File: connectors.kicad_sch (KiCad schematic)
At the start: 44 parts, among them J6 10107844-002LF, J7 JST_XH_1x2_S2B-XH-A-LF-SN, Q5 BC807-25W, SW1 MSS3-V-T_R, U8 USB4145-03-0070-c_REVA2

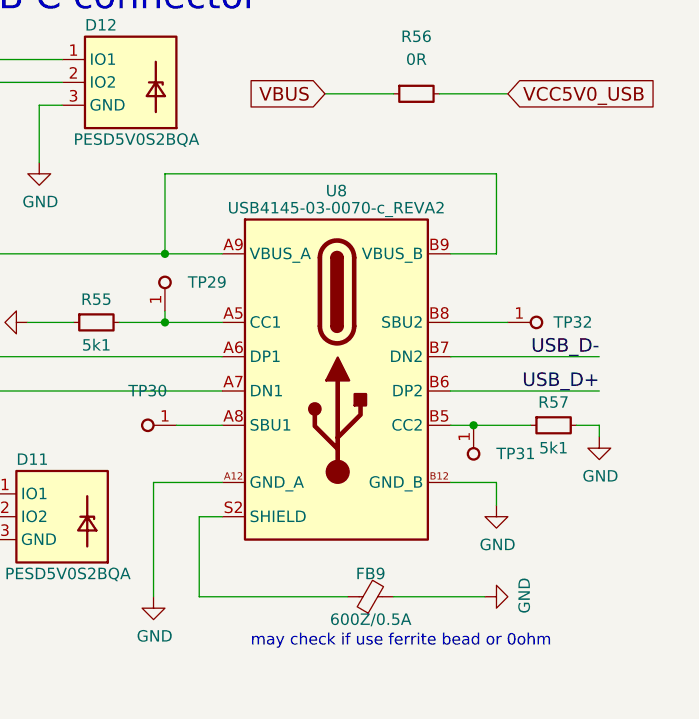
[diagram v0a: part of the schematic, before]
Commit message: Standarize all components and enumerate
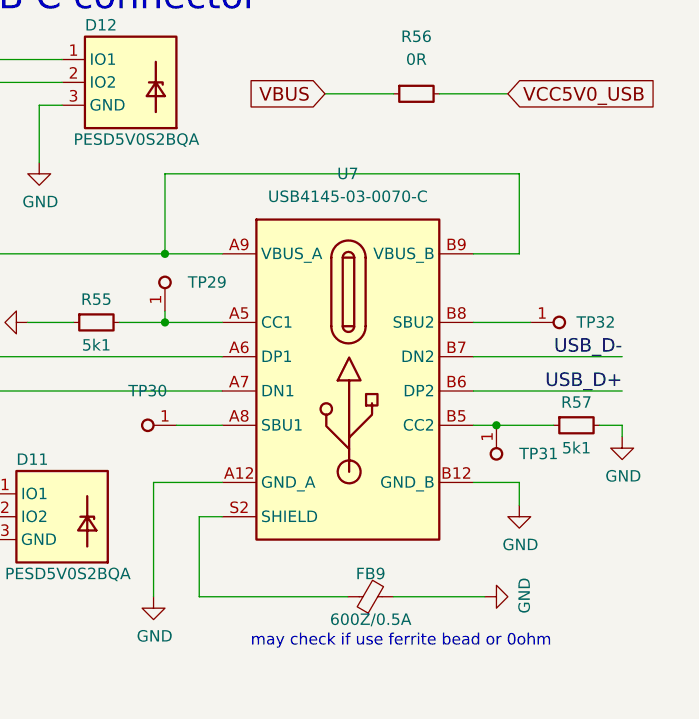
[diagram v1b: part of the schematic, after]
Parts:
- removed U8: USB4145-03-0070-c_REVA2, antmicro-footprints:GCT_USB4145-03-0070-C_REVA, symbol antmicroUSBDVIHDMIConnectors:USB4145-03-0070-c_REVA
- added U7: USB-C_GCT_USB4145-03-0070-C, antmicro-footprints:GCT_USB4145-03-0070-C_REVA, symbol antmicroUSBConnectors:USB-C_GCT_USB4145-03-0070-C
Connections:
- net GND: now also U7.A12 (GND_A), U7.B12 (GND_B)
- net USB_D+: now also U7.A6 (DP1), U7.B6 (DP2)
- net USB_D-: now also U7.A7 (DN1), U7.B7 (DN2)
- net VBUS: now also U7.A9 (VBUS_A), U7.B9 (VBUS_B)
- net at TP32.1: now also U7.B8 (SBU2)
- net at TP30.1: now also U7.A8 (SBU1)
- net at R57.1, TP31.1: now also U7.B5 (CC2)
- net at R55.2, TP29.1: now also U7.A5 (CC1)
- net at FB9.1: now also U7.S2 (SHIELD)
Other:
- moved on the sheet: R57, TP31, TP32

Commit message: Reannotate
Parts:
- renumbered C35 to C38, Q5 to Q8, R50 to R58, R51 to R59, R52 to R60, R53 to R61, R54 to R62, R55 to R63, R56 to R64, R57 to R65, U7 to U10
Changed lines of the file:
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@@
   (symbol (lib_id "antmicroResistorsmisc:R_0R_0805") (at 91.44 179.07 0) (unit 1)
     (in_bom yes) (on_board yes)
-    (property "Reference" "R50" (id 0) (at 93.98 173.99 0)
+    (property "Reference" "R58" (id 0) (at 93.98 173.99 0)
       (effects (font (size 1.27 1.27) (thickness 0.15)))
     )
@@
   (symbol (lib_id "antmicropower:GND") (at 373.38 144.78 0) (unit 1)
     (in_bom yes) (on_board yes)
-    (property "Reference" "#PWR0107" (id 0) (at 373.38 151.13 0)
+    (property "Reference" "#PWR0125" (id 0) (at 373.38 151.13 0)
       (effects (font (size 1.27 1.27)) hide)
     )
@@
   (symbol (lib_id "antmicropower:+3V3") (at 218.44 113.03 0) (unit 1)
     (in_bom yes) (on_board yes) (fields_autoplaced)
-    (property "Reference" "#PWR098" (id 0) (at 233.68 115.57 0)
+    (property "Reference" "#PWR0116" (id 0) (at 233.68 115.57 0)
       (effects (font (size 1.27 1.27) (thickness 0.15)) (justify left bottom) hide)
     )
@@
   (symbol (lib_id "antmicroUSBConnectors:USB-C_GCT_USB4145-03-0070-C") (at 328.93 124.46 0) (unit 1)
     (in_bom yes) (on_board yes) (fields_autoplaced)
-    (property "Reference" "U7" (id 0) (at 342.9 115.57 0)
+    (property "Reference" "U10" (id 0) (at 342.9 115.57 0)
       (effects (font (size 1.27 1.27) (thickness 0.15)))
     )
@@
   (symbol (lib_name "R_0R_0402_2") (lib_id "antmicroResistors0402:R_0R_0402") (at 194.31 143.51 0) (unit 1)
     (in_bom yes) (on_board yes)
-    (property "Reference" "R52" (id 0) (at 196.85 139.7 0)
+    (property "Reference" "R60" (id 0) (at 196.85 139.7 0)
       (effects (font (size 1.27 1.27) (thickness 0.15)))
     )
@@
   (symbol (lib_id "antmicropower:GND") (at 123.19 118.11 0) (unit 1)
     (in_bom yes) (on_board yes)
-    (property "Reference" "#PWR095" (id 0) (at 123.19 124.46 0)
+    (property "Reference" "#PWR0113" (id 0) (at 123.19 124.46 0)
       (effects (font (size 1.27 1.27)) hide)
     )
@@
   (symbol (lib_id "antmicropower:GND") (at 300.99 162.56 0) (unit 1)
     (in_bom yes) (on_board yes)
-    (property "Reference" "#PWR0101" (id 0) (at 300.99 168.91 0)
+    (property "Reference" "#PWR0119" (id 0) (at 300.99 168.91 0)
       (effects (font (size 1.27 1.27)) hide)
     )
@@
   (symbol (lib_id "antmicropower:GND") (at 307.34 132.08 270) (unit 1)
     (in_bom yes) (on_board yes)
-    (property "Reference" "#PWR0102" (id 0) (at 300.99 132.08 0)
+    (property "Reference" "#PWR0120" (id 0) (at 300.99 132.08 0)
       (effects (font (size 1.27 1.27)) hide)
     )
@@
   (symbol (lib_name "R_5k1_0402_1") (lib_id "antmicroResistors0402:R_5k1_0402") (at 365.76 143.51 0) (unit 1)
     (in_bom yes) (on_board yes)
-    (property "Reference" "R57" (id 0) (at 368.3 140.97 0)
+    (property "Reference" "R65" (id 0) (at 368.3 140.97 0)
       (effects (font (size 1.27 1.27) (thickness 0.15)))
     )
@@
   (symbol (lib_id "antmicropower:GND") (at 218.44 147.32 0) (unit 1)
     (in_bom yes) (on_board yes)
-    (property "Reference" "#PWR099" (id 0) (at 218.44 153.67 0)
+    (property "Reference" "#PWR0117" (id 0) (at 218.44 153.67 0)
       (effects (font (size 1.27 1.27)) hide)
     )
@@
   (symbol (lib_name "R_680R_0402_1") (lib_id "antmicroResistors0402:R_680R_0402") (at 218.44 144.78 90) (unit 1)
     (in_bom yes) (on_board yes) (fields_autoplaced)
-    (property "Reference" "R54" (id 0) (at 220.98 140.9699 90)
+    (property "Reference" "R62" (id 0) (at 220.98 140.9699 90)
       (effects (font (size 1.27 1.27) (thickness 0.15)) (justify right))
     )
@@
   (symbol (lib_id "antmicroTransistorsBipolarSingle:BC807-25W") (at 212.09 123.19 0) (mirror x) (unit 1)
     (in_bom yes) (on_board yes) (fields_autoplaced)
-    (property "Reference" "Q5" (id 0) (at 222.25 121.9199 0)
+    (property "Reference" "Q8" (id 0) (at 222.25 121.9199 0)
       (effects (font (size 1.27 1.27) (thickness 0.15)) (justify left))
     )
@@
   (symbol (lib_id "antmicropower:GND") (at 358.14 162.56 90) (unit 1)
     (in_bom yes) (on_board yes)
-    (property "Reference" "#PWR0105" (id 0) (at 364.49 162.56 0)
+    (property "Reference" "#PWR0123" (id 0) (at 364.49 162.56 0)
       (effects (font (size 1.27 1.27)) hide)
     )
@@
   (symbol (lib_name "C_100n_0402_1") (lib_id "antmicroCapacitors0402:C_100n_0402") (at 284.48 130.81 90) (unit 1)
     (in_bom yes) (on_board yes) (fields_autoplaced)
-    (property "Reference" "C35" (id 0) (at 287.02 126.9935 90)
+    (property "Reference" "C38" (id 0) (at 287.02 126.9935 90)
       (effects (font (size 1.27 1.27) (thickness 0.15)) (justify right))
     )
@@
   (symbol (lib_id "antmicropower:GND") (at 284.48 135.89 0) (unit 1)
     (in_bom yes) (on_board yes)
-    (property "Reference" "#PWR0100" (id 0) (at 284.48 142.24 0)
+    (property "Reference" "#PWR0118" (id 0) (at 284.48 142.24 0)
       (effects (font (size 1.27 1.27)) hide)
     )
@@
   (symbol (lib_id "antmicropower:GND") (at 321.31 162.56 0) (unit 1)
     (in_bom yes) (on_board yes)
-    (property "Reference" "#PWR0104" (id 0) (at 321.31 168.91 0)
+    (property "Reference" "#PWR0122" (id 0) (at 321.31 168.91 0)
       (effects (font (size 1.27 1.27)) hide)
     )
@@
   (symbol (lib_id "antmicropower:GND") (at 205.74 147.32 0) (unit 1)
     (in_bom yes) (on_board yes)
-    (property "Reference" "#PWR097" (id 0) (at 205.74 153.67 0)
+    (property "Reference" "#PWR0115" (id 0) (at 205.74 153.67 0)
       (effects (font (size 1.27 1.27)) hide)
     )
@@
   (symbol (lib_name "R_5k1_0402_1") (lib_id "antmicroResistors0402:R_5k1_0402") (at 312.42 132.08 0) (unit 1)
     (in_bom yes) (on_board yes)
-    (property "Reference" "R55" (id 0) (at 314.96 129.54 0)
+    (property "Reference" "R63" (id 0) (at 314.96 129.54 0)
       (effects (font (size 1.27 1.27) (thickness 0.15)))
     )
@@
   (symbol (lib_name "R_0R_0402_1") (lib_id "antmicroResistors0402:R_0R_0402") (at 347.98 106.68 0) (unit 1)
     (in_bom yes) (on_board yes) (fields_autoplaced)
-    (property "Reference" "R56" (id 0) (at 350.52 100.33 0)
+    (property "Reference" "R64" (id 0) (at 350.52 100.33 0)
       (effects (font (size 1.27 1.27) (thickness 0.15)))
     )
@@
   (symbol (lib_id "antmicropower:GND") (at 73.66 120.65 0) (unit 1)
     (in_bom yes) (on_board yes)
-    (property "Reference" "#PWR094" (id 0) (at 73.66 127 0)
+    (property "Reference" "#PWR0112" (id 0) (at 73.66 127 0)
       (effects (font (size 1.27 1.27)) hide)
     )
@@
   (symbol (lib_id "antmicropower:GND") (at 308.61 114.3 0) (unit 1)
     (in_bom yes) (on_board yes)
-    (property "Reference" "#PWR0103" (id 0) (at 308.61 120.65 0)
+    (property "Reference" "#PWR0121" (id 0) (at 308.61 120.65 0)
       (effects (font (size 1.27 1.27)) hide)
     )
@@
   (symbol (lib_id "antmicroResistorsmisc:R_0R_0805") (at 91.44 187.96 0) (unit 1)
     (in_bom yes) (on_board yes)
-    (property "Reference" "R51" (id 0) (at 93.98 182.88 0)
+    (property "Reference" "R59" (id 0) (at 93.98 182.88 0)
       (effects (font (size 1.27 1.27) (thickness 0.15)))
     )
@@
   (symbol (lib_id "antmicropower:GND") (at 361.95 152.4 0) (unit 1)
     (in_bom yes) (on_board yes)
-    (property "Reference" "#PWR0106" (id 0) (at 361.95 158.75 0)
+    (property "Reference" "#PWR0124" (id 0) (at 361.95 158.75 0)
       (effects (font (size 1.27 1.27)) hide)
     )
@@
   (symbol (lib_name "R_10k_0402_1") (lib_id "antmicroResistors0402:R_10k_0402") (at 204.47 123.19 180) (unit 1)
     (in_bom yes) (on_board yes) (fields_autoplaced)
-    (property "Reference" "R53" (id 0) (at 201.93 116.84 0)
+    (property "Reference" "R61" (id 0) (at 201.93 116.84 0)
       (effects (font (size 1.27 1.27) (thickness 0.15)))
     )
@@
   (symbol (lib_id "antmicropower:GND") (at 193.04 135.89 0) (unit 1)
     (in_bom yes) (on_board yes)
-    (property "Reference" "#PWR096" (id 0) (at 193.04 142.24 0)
-      (effects (font (size 1.27 1.27)) hide)
-    )
+    (property "Reference" "#PWR0114" (id 0) (at 193.04 142.24 0)
+      (effects (font (size 1.27 1.27)) hide)
+    )

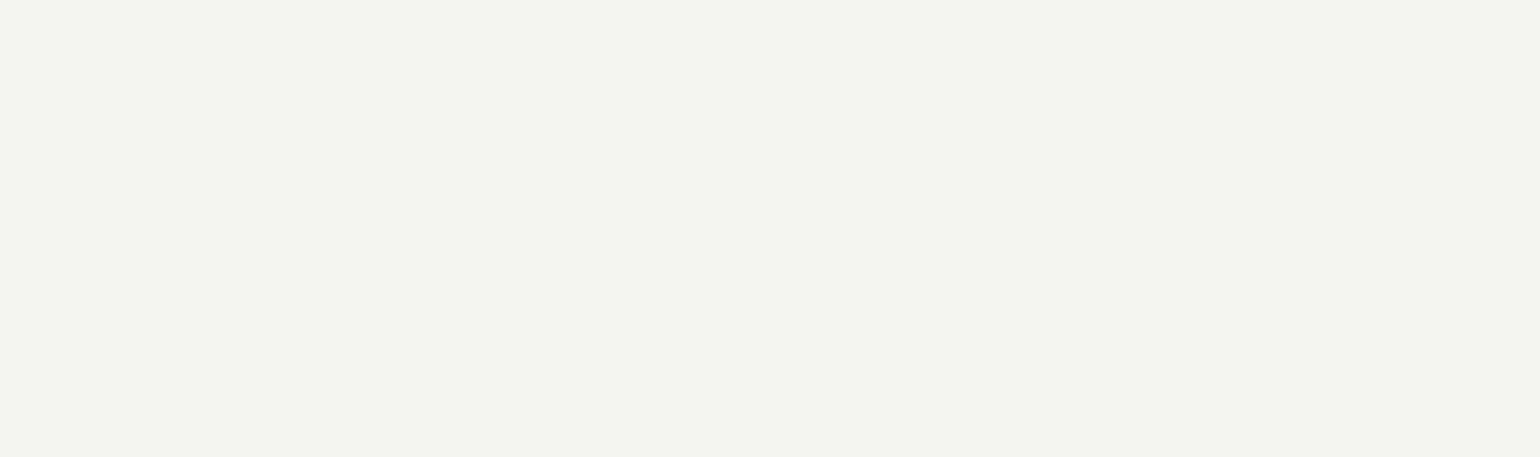
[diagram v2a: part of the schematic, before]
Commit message: Added control circuit for the casing fan
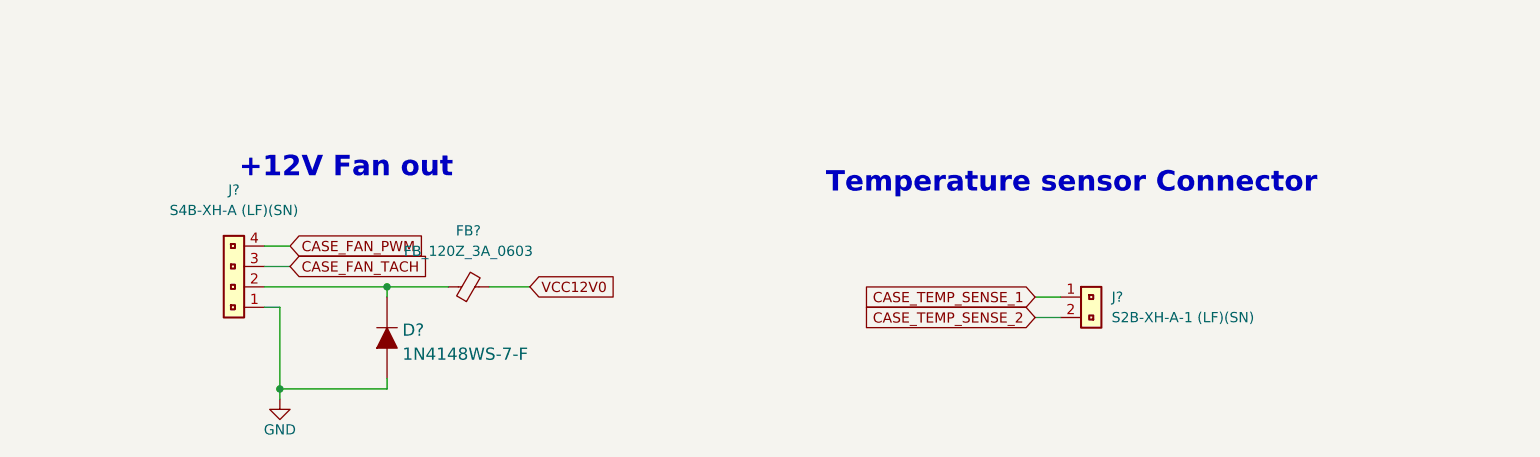
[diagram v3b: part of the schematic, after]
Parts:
- added D?: 1N4148WS-7-F, antmicro-footprints:SOD-323, symbol antmicroDiodesRectifiersSingle:1N4148WS-7-F
- added FB?: FB_120Z_3A_0603, antmicro-footprints:FB_0603_1608Metric, symbol antmicroFerriteBeadsandChips:FB_120Z_3A_0603
- added J?: PinHeader_1x4_P2.5mm_Drill1mm_Horizontal_Shrouded, antmicro-footprints:PinHeader_1x4_P2.5mm_Drill1mm_Horizontal_Shrouded, symbol antmicroRectangularConnectorsHeadersMalePins:PinHeader_1x4_P2.5mm_Drill1mm_Hori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
- added J?: PinHeader_1x2_P2.5mm_Drill1mm_Horizontal_Shrouded, antmicro-footprints:PinHeader_1x2_P2.5mm_Drill1mm_Horizontal_Shrouded, symbol antmicroRectangularConnectorsHeadersMalePins:PinHeader_1x2_P2.5mm_Drill1mm_Hori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
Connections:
- net GND: now also D?.A, J?.1
- net VCC12V0: now also FB?.2
- new net: D?.K, FB?.1, J?.2
- new net CASE_FAN_PWM: J?.4
- new net CASE_FAN_TACH: J?.3
- new net CASE_TEMP_SENSE_1: J?.1
- new net CASE_TEMP_SENSE_2: J?.2
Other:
- note added: "+12V Fan out"
- note added: "Temperature sensor Connector"

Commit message: Cosmetic changes and added adnotations
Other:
- note added: "need to validate this during bringup as we don't know current capabilities of the 12V always on output"
- note added: "on PCB leave about 1cm space around this connector as additional part strenghtening it will be designed"
- moved on the sheet: FB?
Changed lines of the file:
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@@
     (stroke (width 0) (type default) (color 0 0 0 0))
   )
-  (wire (pts (xy 210.82 214.63) (xy 218.44 214.63))
+  (wire (pts (xy 210.82 214.63) (xy 222.25 214.63))
     (stroke (width 0) (type default) (color 0 0 0 0))
   )
@@
     (stroke (width 0) (type default) (color 0 0 0 0))
   )
-  (wire (pts (xy 361.95 115.57) (xy 322.58 115.57))
+  (wire (pts (xy 361.95 113.665) (xy 322.58 113.665))
     (stroke (width 0) (type default) (color 0 0 0 0))
   )
@@
     (stroke (width 0) (type default) (color 0 0 0 0))
   )
-  (wire (pts (xy 223.52 214.63) (xy 228.6 214.63))
+  (wire (pts (xy 227.33 214.63) (xy 228.6 214.63))
     (stroke (width 0) (type default) (color 0 0 0 0))
   )
@@
     (stroke (width 0) (type default) (color 0 0 0 0))
   )
-  (wire (pts (xy 322.58 115.57) (xy 322.58 124.46))
+  (wire (pts (xy 322.58 113.665) (xy 322.58 124.46))
     (stroke (width 0) (type default) (color 0 0 0 0))
   )
@@
     (stroke (width 0) (type default) (color 0 0 0 0))
   )
-  (wire (pts (xy 361.95 124.46) (xy 361.95 115.57))
+  (wire (pts (xy 361.95 124.46) (xy 361.95 113.665))
     (stroke (width 0) (type default) (color 0 0 0 0))
   )
@@
     )
   )
+  (text "on PCB leave about 1cm space around \nthis connector as additional part \nstrenghtening it will be designed"
+    (at 363.855 127 0)
+    (effects (font (size 1.27 1.27)) (justify left bottom))
+  )
   (text "Dell D1600e PSU connector" (at 66.675 94.615 0)
     (effects (font (size 2.9972 2.9972)) (justify left bottom))
@@
     (effects (font (size 2.9972 2.9972)) (justify left bottom))
   )
+  (text "need to validate this during bringup\nas we don't know current capabilities\nof the 12V always on output"
+    (at 76.835 196.85 0)
+    (effects (font (size 1.27 1.27)) (justify left bottom))
+  )
   (text "may check if use ferrite bead or 0ohm" (at 332.105 168.275 0)
     (effects (font (size 1.27 1.27)) (justify left bottom))
@@
     (pin "1")
   )
-  (symbol (lib_id "antmicroFerriteBeadsandChips:FB_120Z_3A_0603") (at 218.44 214.63 0) (unit 1)
+  (symbol (lib_id "antmicroFerriteBeadsandChips:FB_120Z_3A_0603") (at 222.25 214.63 0) (unit 1)
     (in_bom yes) (on_board yes) (fields_autoplaced)
-    (property "Reference" "FB?" (id 0) (at 220.9419 207.645 0)
+    (property "Reference" "FB?" (id 0) (at 224.7519 207.645 0)
       (effects (font (size 1.27 1.27) (thickness 0.15)))
     )
-    (property "Value" "FB_120Z_3A_0603" (id 1) (at 220.9419 210.185 0)
+    (property "Value" "FB_120Z_3A_0603" (id 1) (at 224.7519 210.185 0)
       (effects (font (size 1.27 1.27) (thickness 0.15)))
     )
-    (property "Footprint" "antmicro-footprints:FB_0603_1608Metric" (id 2) (at 232.41 219.71 0)
+    (property "Footprint" "antmicro-footprints:FB_0603_1608Metric" (id 2) (at 236.22 219.71 0)
       (effects (font (size 1.27 1.27) (thickness 0.15)) (justify left bottom) hide)
     )
-    (property "Datasheet" "https://www.murata.com/en-global/api/pdfdownloadapi?cate=luNoiseSupprFilteChipFerriBead&partno=BLM18SG121TN1%23" (id 3) (at 232.41 222.25 0)
+    (property "Datasheet" "https://www.murata.com/en-global/api/pdfdownloadapi?cate=luNoiseSupprFilteChipFerriBead&partno=BLM18SG121TN1%23" (id 3) (at 236.22 222.25 0)
       (effects (font (size 1.27 1.27) (thickness 0.15)) (justify left bottom) hide)
     )
-    (property "MPN" "BLM18SG121TN1D" (id 4) (at 232.41 224.79 0)
+    (property "MPN" "BLM18SG121TN1D" (id 4) (at 236.22 224.79 0)
       (effects (font (size 1.27 1.27) (thickness 0.15)) (justify left bottom) hide)
     )
-    (property "Manufacturer" "Murata" (id 5) (at 232.41 227.33 0)
+    (property "Manufacturer" "Murata" (id 5) (at 236.22 227.33 0)
       (effects (font (size 1.27 1.27) (thickness 0.15)) (justify left bottom) hide)
     )
-    (property "Author" "Antmicro" (id 6) (at 232.41 229.87 0)
+    (property "Author" "Antmicro" (id 6) (at 236.22 229.87 0)
       (effects (font (size 1.27 1.27) (thickness 0.15)) (justify left bottom) hide)
     )
-    (property "License" "Apache-2.0" (id 7) (at 232.41 232.41 0)
+    (property "License" "Apache-2.0" (id 7) (at 236.22 232.41 0)
       (effects (font (size 1.27 1.27) (thickness 0.15)) (justify left bottom) hide)
     )

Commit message: Additional cleanup
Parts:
- gave numbers to parts that had none: 4
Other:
- title: (none) -> GPU Cluster Backplane
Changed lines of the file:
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@@
   (paper "A3")
   (title_block
+    (title "GPU Cluster Backplane")
+    (date "2023-10-18")
     (rev "1.0.0")
     (comment 1 "www.antmicro.com")
@@
   (symbol (lib_id "antmicropower:GND") (at 197.485 228.6 0) (unit 1)
     (in_bom yes) (on_board yes)
-    (property "Reference" "#PWR?" (id 0) (at 197.485 234.95 0)
+    (property "Reference" "#PWR0380" (id 0) (at 197.485 234.95 0)
       (effects (font (size 1.27 1.27)) hide)
     )
@@
   (symbol (lib_id "antmicroFerriteBeadsandChips:FB_120Z_3A_0603") (at 222.25 214.63 0) (unit 1)
     (in_bom yes) (on_board yes) (fields_autoplaced)
-    (property "Reference" "FB?" (id 0) (at 224.7519 207.645 0)
+    (property "Reference" "FB17" (id 0) (at 224.7519 207.645 0)
       (effects (font (size 1.27 1.27) (thickness 0.15)))
     )
@@
   (symbol (lib_id "antmicroDiodesRectifiersSingle:1N4148WS-7-F") (at 210.82 220.98 90) (unit 1)
     (in_bom yes) (on_board yes) (fields_autoplaced)
-    (property "Reference" "D?" (id 0) (at 212.725 220.0038 90)
+    (property "Reference" "D46" (id 0) (at 212.725 220.0038 90)
       (effects (font (size 1.524 1.524)) (justify right))
     )
@@
   (symbol (lib_id "antmicroRectangularConnectorsHeadersMalePins:PinHeader_1x4_P2.5mm_Drill1mm_Horizontal_Shrouded") (at 195.58 217.17 180) (unit 1)
     (in_bom yes) (on_board yes) (fields_autoplaced)
-    (property "Reference" "J?" (id 0) (at 191.77 202.565 0)
+    (property "Reference" "J18" (id 0) (at 191.77 202.565 0)
       (effects (font (size 1.27 1.27) (thickness 0.15)))
     )
@@
   (symbol (lib_id "antmicroRectangularConnectorsHeadersMalePins:PinHeader_1x2_P2.5mm_Drill1mm_Horizontal_Shrouded") (at 294.64 215.9 0) (unit 1)
     (in_bom yes) (on_board yes) (fields_autoplaced)
-    (property "Reference" "J?" (id 0) (at 300.99 215.8999 0)
+    (property "Reference" "J19" (id 0) (at 300.99 215.8999 0)
       (effects (font (size 1.27 1.27) (thickness 0.15)) (justify left))
     )
